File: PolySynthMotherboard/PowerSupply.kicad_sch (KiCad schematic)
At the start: 61 parts, among them J502 BATTERY, J502 POWER, Q701 BSH205G2A, Q702 TD6790, Q703 TD6790, Q704 TD6790, U503 CS5173, U702 TC7662Bx0A, U703 MCP73834T, U704 TPS63021, U705 TC7662Bx0A

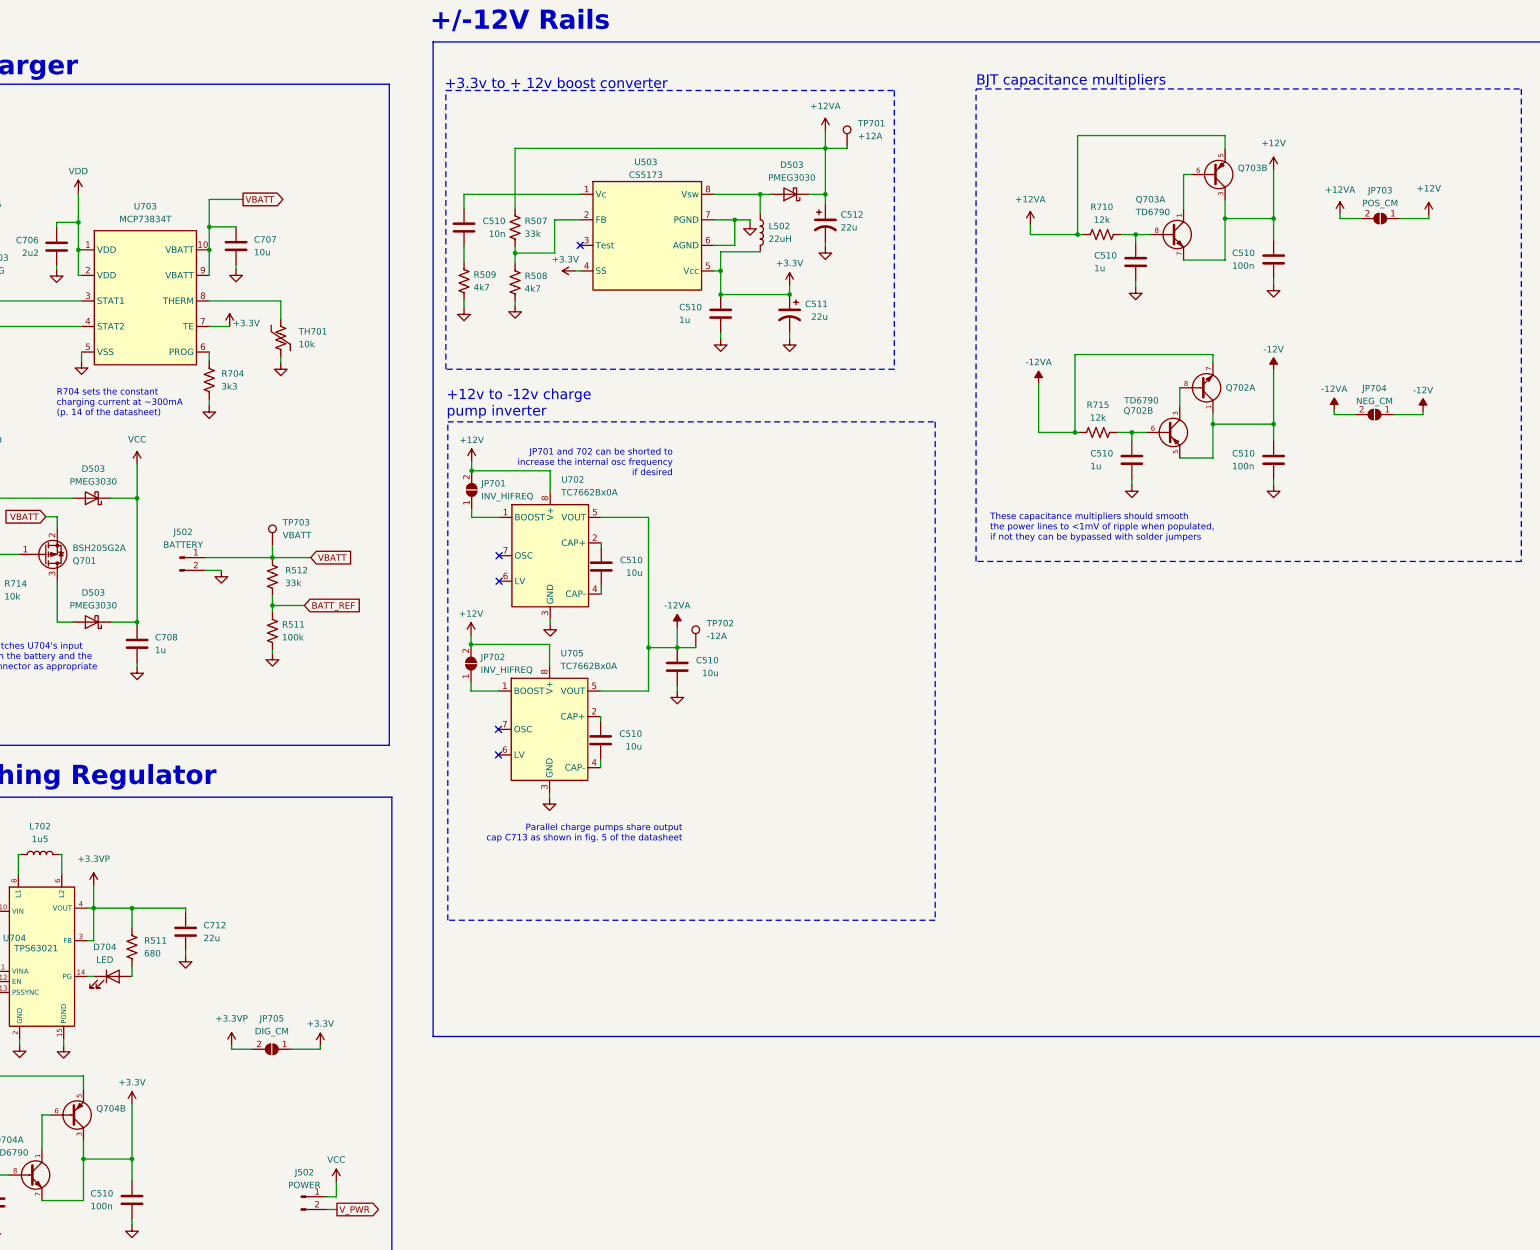
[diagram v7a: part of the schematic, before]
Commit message: footprints placed
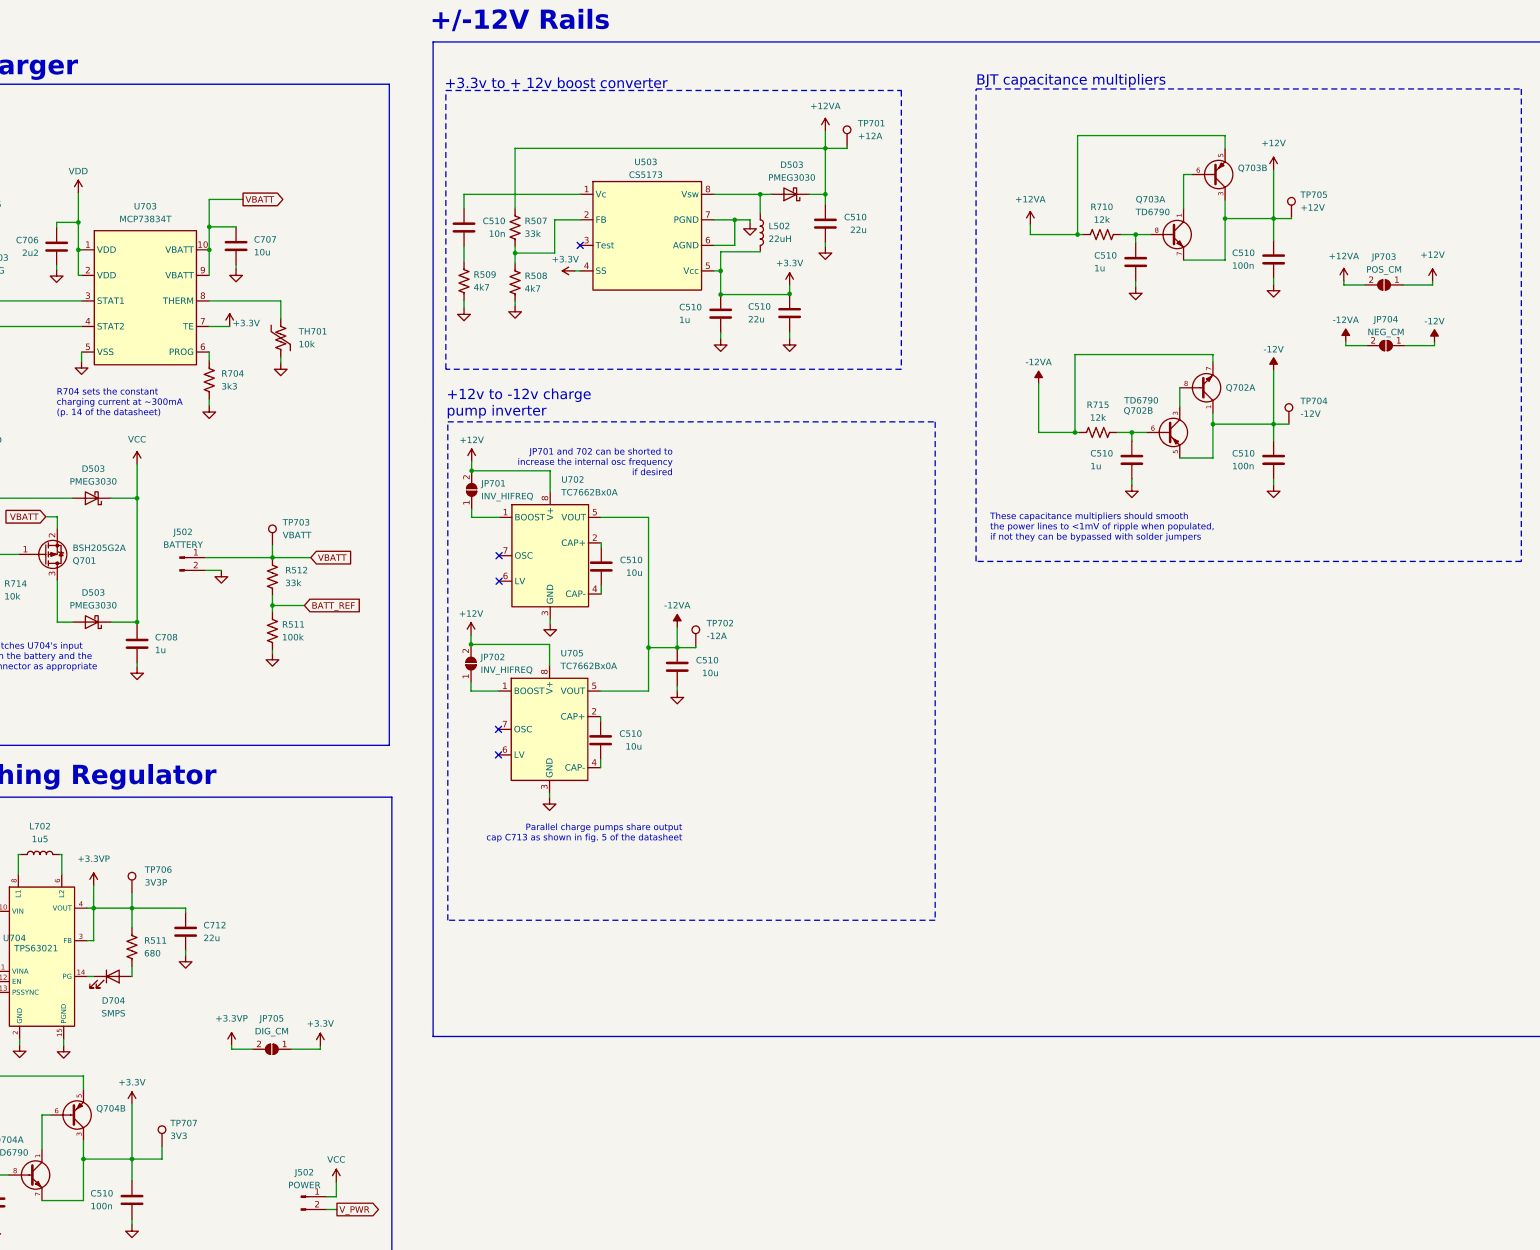
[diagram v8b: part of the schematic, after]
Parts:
- removed C511, C512: 22u, Capacitor_THT:CP_Radial_D4.0mm_P2.00mm, symbol Device:C_Polarized_US
- added C510 (x2): 22u, Capacitor_SMD:C_0805_2012Metric, symbol Device:C
- added TP704: -12V, TestPoint:TestPoint_Pad_D1.0mm_Value, symbol Connector:TestPoint
- added TP705: +12V, TestPoint:TestPoint_Pad_D1.0mm_Value, symbol Connector:TestPoint
- added TP706: 3V3P, TestPoint:TestPoint_Pad_D1.0mm_Value, symbol Connector:TestPoint
- added TP707: 3V3, TestPoint:TestPoint_Pad_D1.0mm_Value, symbol Connector:TestPoint
- D704: value LED -> SMPS
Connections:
- net V_PWR is gone; now on net VIN: C709.1, C710.1, C711.1, J502.2 (Pin_2), U704.1 (VINA), U704.10 (VIN), U704.12 (EN), U704.13 (PSSYNC)
- net +12V: now also TP705.1
- net +12VA: now also C510.1
- net +3.3V: now also C510.1, TP707.1
- net +3.3VP: now also U704.5 (VOUT), TP706.1
- net -12V: now also TP704.1
- net GND: now also C510.2, C510.2
- net at L702.1, U704.8 (L1): now also U704.9 (L1)
- net at L702.2, U704.6 (L2): now also U704.7 (L2)
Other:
- moved on the sheet: JP703, JP704
